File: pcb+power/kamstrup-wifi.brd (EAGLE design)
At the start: 36 x 81.3 mm, 24 parts, among them T1 BT137S-600D, T2 BT137S-600D

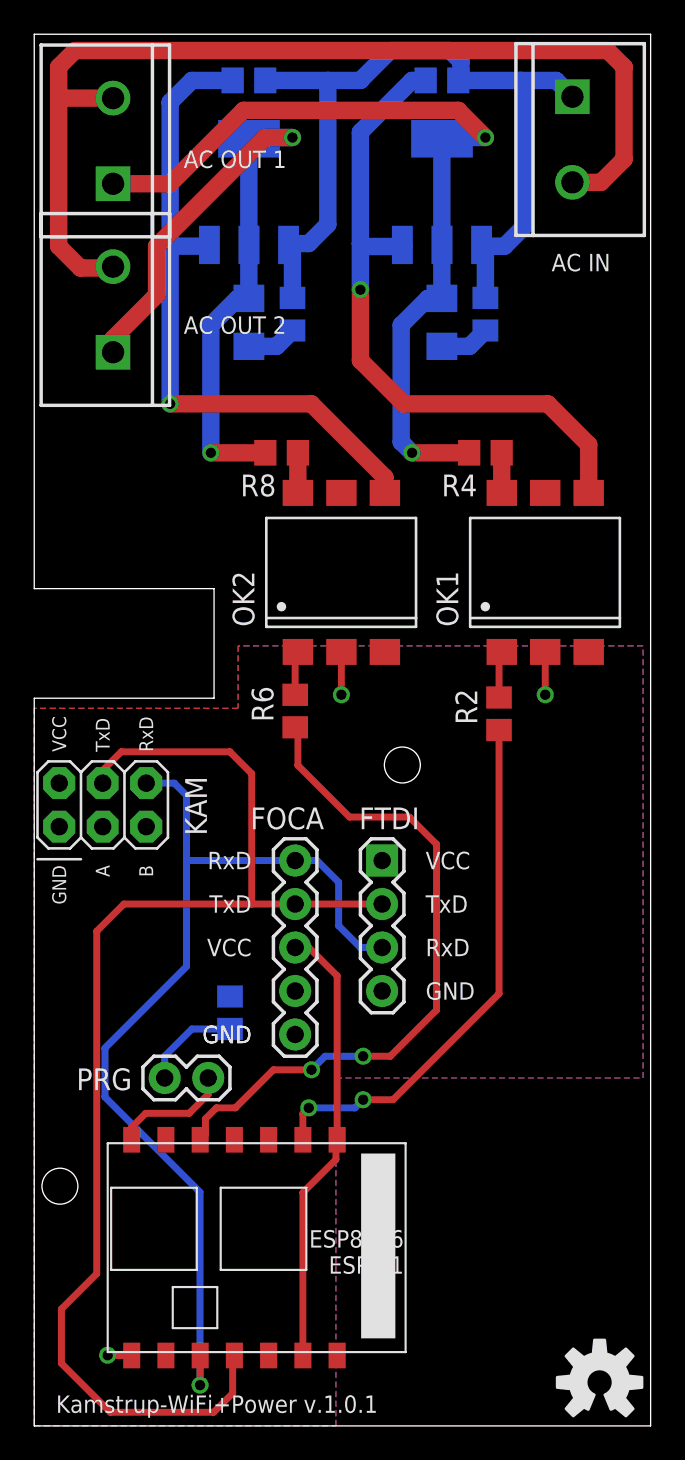
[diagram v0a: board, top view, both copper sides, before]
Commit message: pcb v.1.1
triac sot428 + esp-07 pin layout
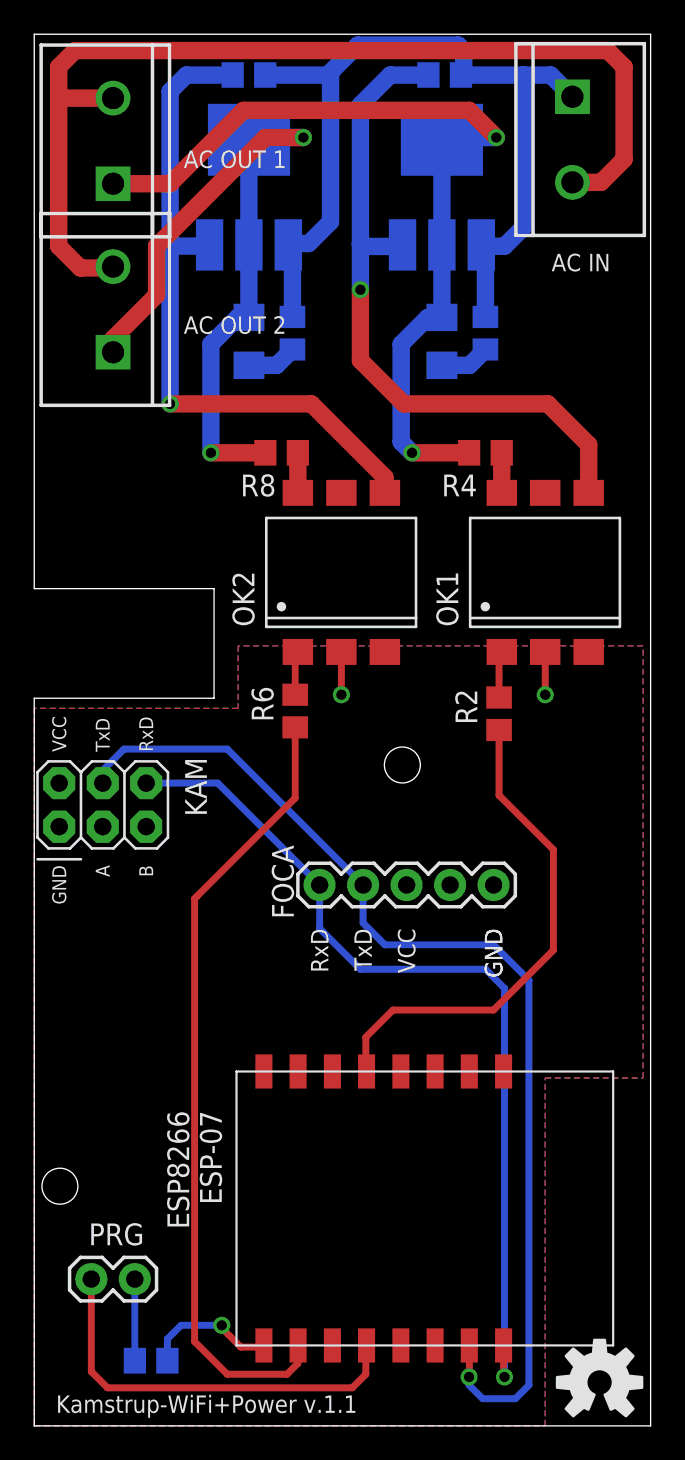
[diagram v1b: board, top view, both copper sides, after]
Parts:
- removed FTDI: (no value), SparkFun-Connectors:1X04
- removed U$3: ESP8266-03, ESP8266:ESP-03
- added U$1: ESP8266-07, lio:ESP-07
- OK1, OK2: value MOC3043S -> MOC3063S
- T1, T2: value BT137S-600D -> BT137; device SparkFun (old):SOT223 -> Triac SOT428:SOT428
- moved R1 20.8 mm to (6.83, 3.81), turned to 0 degrees
- moved PRG 11.9 mm to (5.87, 8.57), turned to 180 degrees
- moved FOCA 2.02 mm to (16.7, 31.6), turned to 0 degrees
- moved C1 1.11 mm to (23.8, 63.3)
- moved C2 1.11 mm to (12.5, 63.3)
- moved R5 1.11 mm to (26.4, 63.8)
- moved R9 1.11 mm to (15.1, 63.8)
- moved R3 0.35 mm to (24.0, 78.9)
- moved R7 0.32 mm to (12.5, 78.9)
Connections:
- net 3.3V: now also U$1.CH_PD, U$1.VCC; no longer FTDI.1, U$3.CH_PD, U$3.VCC
- net GND: now also U$1.GND; no longer FTDI.4, U$3.GND
- net N$1: now also U$1.TXD; no longer FTDI.3, U$3.UTXD
- net N$11: now also U$1.GPIO14; no longer U$3.GPIO14
- net N$15: now also T1.4; no longer T1.2
- net N$16: now also U$1.GPIO15; no longer U$3.GPIO15
- net N$2: now also U$1.RXD; no longer FTDI.2, U$3.URXD
- net N$3: now also U$1.GPIO0; no longer U$3.GPIO0
- net N$8: now also T2.4; no longer T2.2
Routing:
- net 3.3V: track 26.2 -> 0.00 mm
- net N$3: track 6.95 -> 23.8 mm
- net N$2: track 75.6 -> 63.2 mm, vias 0 -> 1
- net GND: track 6.41 -> 14.2 mm
- net N$1: track 58.5 -> 51.9 mm
- net N$16: track 39.9 -> 46.5 mm, vias 2 -> 0
- net N$9: track 50.1 -> 52.4 mm
- net N$11: track 31.3 -> 29.3 mm, vias 2 -> 0
- net N$8: track 43.3 -> 44.5 mm
- net N$15: track 50.2 -> 51.3 mm
- net N$13: track 39.3 -> 40.4 mm
- net N$4: track 5.74 -> 4.76 mm
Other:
- board text added: "ESP8266 ESP-07"
- board text added: "Kamstrup-WiFi+Power v.1.1"
- board text removed: "ESP8266 ESP-01"
- board text removed: "Kamstrup-WiFi+Power v.1.0.1"

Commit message: pcb: v.1.1.1
larger triac footprint + writable area
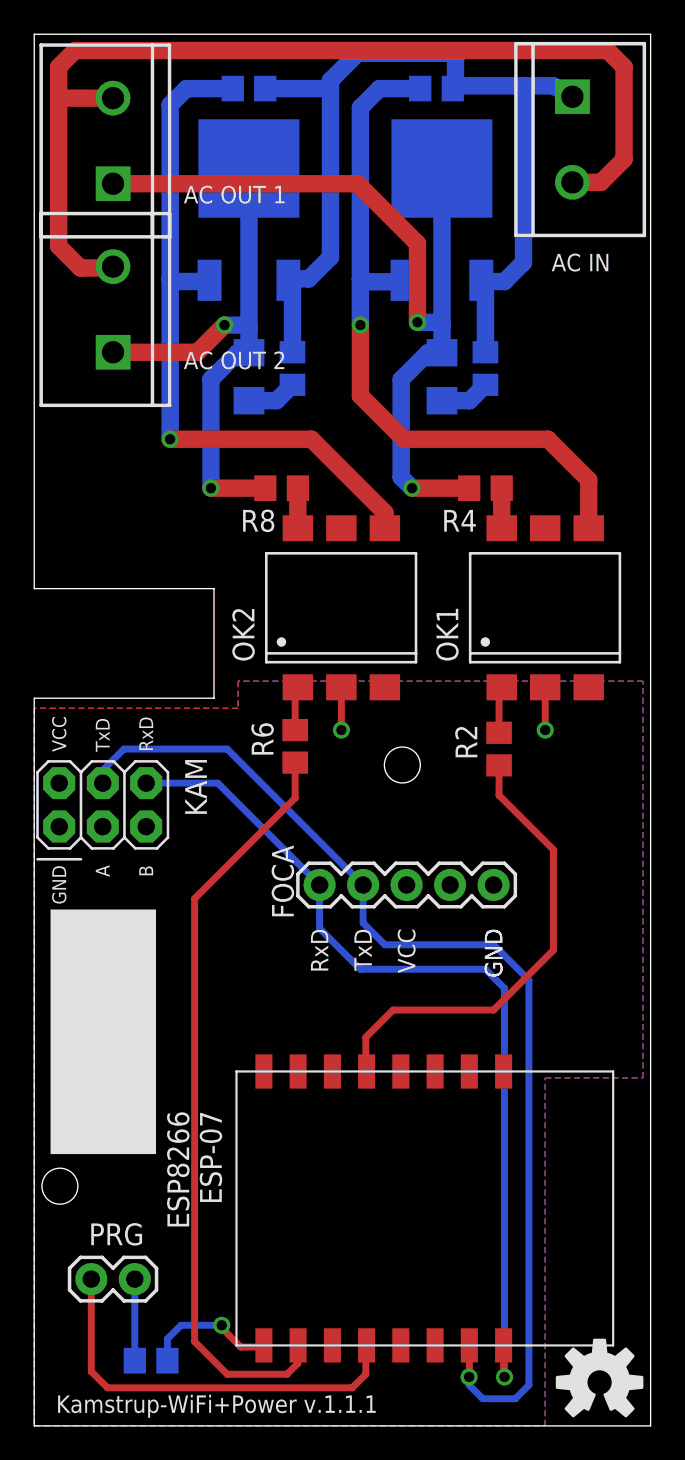
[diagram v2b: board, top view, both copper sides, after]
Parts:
- moved R4 2.06 mm to (26.4, 54.8)
- moved R5 2.06 mm to (26.4, 61.8)
- moved R8 2.06 mm to (14.4, 54.8)
- moved R9 2.06 mm to (15.1, 61.8)
- moved C1 2.06 mm to (23.8, 61.3)
- moved C2 2.06 mm to (12.5, 61.3)
- moved OK1 2.06 mm to (29.8, 47.8)
- moved OK2 2.06 mm to (17.9, 47.8)
- moved R2 2.06 mm to (27.1, 39.5)
- moved R6 2.06 mm to (15.2, 39.7)
- moved T1 2.06 mm to (23.8, 70.0)
- moved T2 2.06 mm to (12.5, 70.0)
- moved R3 0.93 mm to (23.5, 78.1)
- moved R7 0.79 mm to (12.5, 78.1)
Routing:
- net N$8: track 44.5 -> 31.6 mm
- net N$9: track 52.4 -> 55.2 mm
- net N$15: track 51.3 -> 49.1 mm
- net N$16: track 46.5 -> 44.4 mm
- net N$11: track 29.3 -> 27.2 mm
- net N$6: track 39.8 -> 41.1 mm
- net N$13: track 40.4 -> 41.6 mm
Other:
- board text added: "Kamstrup-WiFi+Power v.1.1.1"
- board text removed: "Kamstrup-WiFi+Power v.1.1"
